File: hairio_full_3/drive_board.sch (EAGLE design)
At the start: 29 parts, among them J1 105313-1104, J2 105313-1104, P1 S2B-PH-SM4-TB(LF)(SN), P2 S2B-PH-SM4-TB(LF)(SN)

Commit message: update board
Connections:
- net A0: now also ARDUINO_NANO1.ADC3/A3; no longer ARDUINO_NANO1.ADC0/A0
- net A1_THERM_1: now also ARDUINO_NANO1.ADC0/A0; no longer ARDUINO_NANO1.ADC1/A1
- net A2_THERM_2: now also ARDUINO_NANO1.ADC1/A1; no longer ARDUINO_NANO1.ADC2/A2
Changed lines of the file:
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@@
 </class>
 <class number="1" name="isolation" width="0" drill="0">
-<clearance class="1" value="0.4064"/>
 </class>
 </classes>
@@
 </segment>
 <segment>
-<pinref part="ARDUINO_NANO1" gate="G$1" pin="ADC0/A0"/>
-<wire x1="203.2" y1="99.06" x2="213.36" y2="99.06" width="0.1524" layer="91"/>
-<label x="213.36" y="96.52" size="1.778" layer="95"/>
+<pinref part="ARDUINO_NANO1" gate="G$1" pin="ADC3/A3"/>
+<wire x1="203.2" y1="106.68" x2="210.82" y2="106.68" width="0.1524" layer="91"/>
+<label x="210.82" y="106.68" size="1.778" layer="95"/>
 </segment>
 </net>
@@
 <net name="A2_THERM_2" class="0">
 <segment>
-<pinref part="ARDUINO_NANO1" gate="G$1" pin="ADC2/A2"/>
-<wire x1="203.2" y1="104.14" x2="213.36" y2="104.14" width="0.1524" layer="91"/>
-<label x="213.36" y="104.14" size="1.778" layer="95"/>
-</segment>
-<segment>
 <wire x1="-71.12" y1="88.9" x2="-71.12" y2="83.82" width="0.1524" layer="91"/>
 <label x="-71.12" y="60.96" size="1.778" layer="95" rot="R90"/>
@@
 <junction x="-71.12" y="83.82"/>
 </segment>
+<segment>
+<pinref part="ARDUINO_NANO1" gate="G$1" pin="ADC1/A1"/>
+<wire x1="203.2" y1="101.6" x2="210.82" y2="101.6" width="0.1524" layer="91"/>
+<label x="213.36" y="101.6" size="1.778" layer="95"/>
+</segment>
 </net>
 <net name="A1_THERM_1" class="1">
-<segment>
-<pinref part="ARDUINO_NANO1" gate="G$1" pin="ADC1/A1"/>
-<wire x1="203.2" y1="101.6" x2="213.36" y2="101.6" width="0.1524" layer="91"/>
-<label x="213.36" y="101.6" size="1.778" layer="95"/>
-</segment>
 <segment>
 <wire x1="38.1" y1="88.9" x2="38.1" y2="83.82" width="0.1524" layer="91"/>
@@
 <junction x="38.1" y="83.82"/>
 </segment>
-</net>
+<segment>
+<pinref part="ARDUINO_NANO1" gate="G$1" pin="ADC0/A0"/>
+<wire x1="203.2" y1="99.06" x2="210.82" y2="99.06" width="0.1524" layer="91"/>
+<label x="210.82" y="96.52" size="1.778" layer="95"/>
+</segment>
+</net>

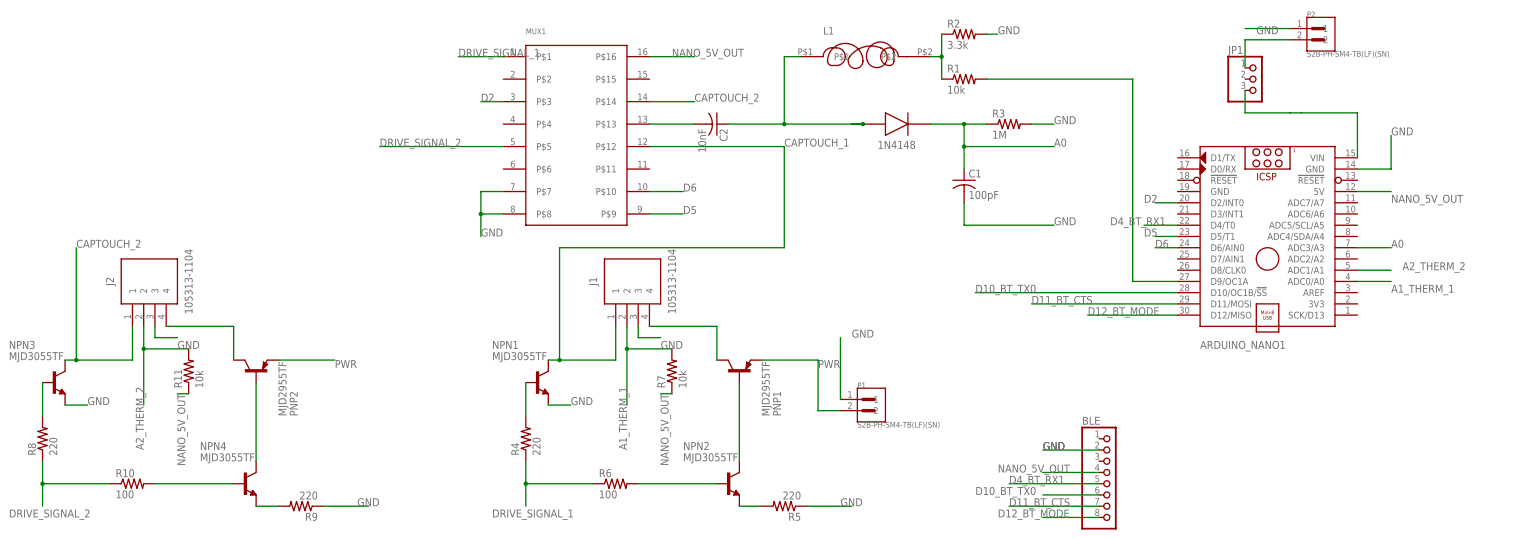
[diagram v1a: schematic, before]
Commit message: new board -- the dimensioned version of what got made for demos (with ground plane fix after accidental deletion)
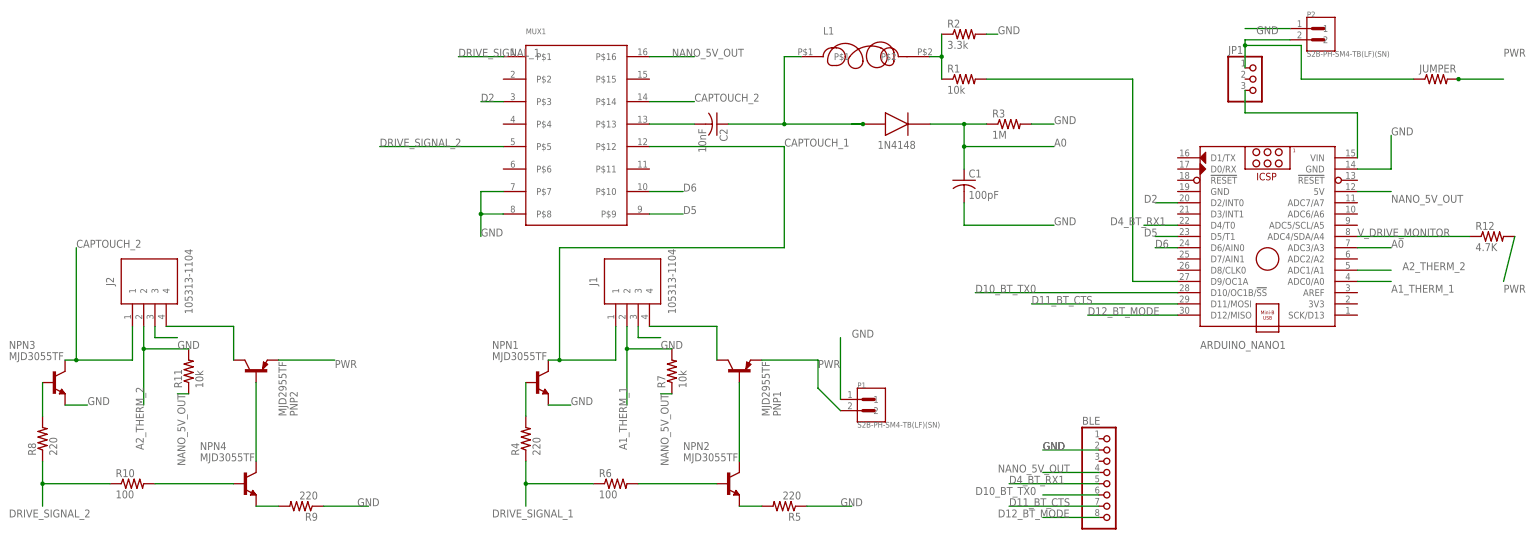
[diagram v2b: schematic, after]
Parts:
- added JUMPER: (no value), resistor:R-US_R0805
- added R12: 4.7K, resistor:R-US_R0805
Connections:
- new net V_DRIVE_MONITOR: ARDUINO_NANO1.ADC4/SDA/A4, R12.1
- net N$16: now also JUMPER.1
- net PWR: now also JUMPER.2, R12.2
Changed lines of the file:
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@@
 <part name="J2" library="105313-1104" deviceset="105313-1104" device=""/>
 <part name="JP1" library="pinhead" deviceset="PINHD-1X3" device=""/>
+<part name="R12" library="resistor" deviceset="R-US_" device="R0805" value="4.7K"/>
+<part name="JUMPER" library="resistor" deviceset="R-US_" device="R0805"/>
 </parts>
 <sheets>
@@
 <instance part="J2" gate="G$1" x="-73.66" y="88.9" rot="R90"/>
 <instance part="JP1" gate="A" x="180.34" y="144.78"/>
+<instance part="R12" gate="G$1" x="233.68" y="109.22"/>
+<instance part="JUMPER" gate="G$1" x="220.98" y="144.78"/>
 </instances>
 <busses>
@@
 <net name="PWR" class="0">
 <segment>
+<pinref part="PNP2" gate="G$1" pin="E"/>
+<wire x1="-40.64" y1="81.28" x2="-27.94" y2="81.28" width="0.1524" layer="91"/>
+<label x="-27.94" y="81.28" size="1.778" layer="95" rot="MR180"/>
+</segment>
+<segment>
+<pinref part="R12" gate="G$1" pin="2"/>
+<wire x1="238.76" y1="109.22" x2="236.22" y2="99.06" width="0.1524" layer="91"/>
+<label x="236.22" y="96.52" size="1.778" layer="95"/>
+</segment>
+<segment>
+<pinref part="JUMPER" gate="G$1" pin="2"/>
+<wire x1="226.06" y1="144.78" x2="236.22" y2="144.78" width="0.1524" layer="91"/>
+<label x="236.22" y="149.86" size="1.778" layer="95"/>
+<junction x="226.06" y="144.78"/>
+</segment>
+<segment>
 <pinref part="PNP1" gate="G$1" pin="E"/>
 <wire x1="68.58" y1="81.28" x2="81.28" y2="81.28" width="0.1524" layer="91"/>
 <label x="81.28" y="81.28" size="1.778" layer="95" rot="MR180"/>
 <pinref part="P1" gate="G$1" pin="2"/>
-<wire x1="86.36" y1="69.85" x2="81.28" y2="69.85" width="0.1524" layer="91"/>
-<wire x1="81.28" y1="69.85" x2="81.28" y2="81.28" width="0.1524" layer="91"/>
-</segment>
-<segment>
-<pinref part="PNP2" gate="G$1" pin="E"/>
-<wire x1="-40.64" y1="81.28" x2="-27.94" y2="81.28" width="0.1524" layer="91"/>
-<label x="-27.94" y="81.28" size="1.778" layer="95" rot="MR180"/>
+<wire x1="81.28" y1="81.28" x2="81.28" y2="74.93" width="0.1524" layer="91"/>
+<wire x1="81.28" y1="74.93" x2="86.36" y2="69.85" width="0.1524" layer="91"/>
 </segment>
 </net>
@@
 <pinref part="ARDUINO_NANO1" gate="G$1" pin="VIN"/>
 <wire x1="203.2" y1="127" x2="203.2" y2="137.16" width="0.1524" layer="91"/>
-<wire x1="203.2" y1="137.16" x2="190.5" y2="137.16" width="0.1524" layer="91"/>
+<wire x1="203.2" y1="137.16" x2="177.8" y2="137.16" width="0.1524" layer="91"/>
 <pinref part="JP1" gate="A" pin="3"/>
-<wire x1="190.5" y1="137.16" x2="187.96" y2="137.16" width="0.1524" layer="91"/>
 <wire x1="177.8" y1="142.24" x2="177.8" y2="137.16" width="0.1524" layer="91"/>
-<wire x1="177.8" y1="137.16" x2="187.96" y2="137.16" width="0.1524" layer="91"/>
 </segment>
 </net>
@@
 <pinref part="JP1" gate="A" pin="1"/>
 <pinref part="P2" gate="G$1" pin="2"/>
-<wire x1="177.8" y1="147.32" x2="177.8" y2="153.67" width="0.1524" layer="91"/>
+<wire x1="177.8" y1="147.32" x2="177.8" y2="152.4" width="0.1524" layer="91"/>
+<wire x1="177.8" y1="152.4" x2="177.8" y2="153.67" width="0.1524" layer="91"/>
 <wire x1="177.8" y1="153.67" x2="187.96" y2="153.67" width="0.1524" layer="91"/>
-</segment>
-</net>
+<pinref part="JUMPER" gate="G$1" pin="1"/>
+<wire x1="215.9" y1="144.78" x2="190.5" y2="144.78" width="0.1524" layer="91"/>
+<wire x1="190.5" y1="144.78" x2="190.5" y2="152.4" width="0.1524" layer="91"/>
+<wire x1="190.5" y1="152.4" x2="177.8" y2="152.4" width="0.1524" layer="91"/>
+<junction x="177.8" y="152.4"/>
+</segment>
+</net>
+<net name="V_DRIVE_MONITOR" class="0">
+<segment>
+<pinref part="ARDUINO_NANO1" gate="G$1" pin="ADC4/SDA/A4"/>
+<wire x1="203.2" y1="109.22" x2="228.6" y2="109.22" width="0.1524" layer="91"/>
+<label x="203.2" y="109.22" size="1.778" layer="95"/>
+<pinref part="R12" gate="G$1" pin="1"/>
+</segment>
+</net>
